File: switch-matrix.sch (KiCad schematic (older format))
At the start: 31 parts, among them P1 SW_0, P2 SW_1, P3 SW_2, P4 SW_3, Q1 NPN, Q2 NPN, Q3 NPN, Q4 NPN, U1 74HC14

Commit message: changed the controller adding some shift registers
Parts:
- renumbered C2 to C1, C3 to C2, C4 to C3, C5 to C4, C1 to C5, D5 to D1, D2 to D10, D3 to D11, D4 to D12, D7 to D2, D9 to D3, D11 to D4, D6 to D5, D8 to D6, D10 to D7, D12 to D8, D1 to D9, P3 to P2, P2 to P3, RP3 to RP2, RP5 to RP3, RP2 to RP5
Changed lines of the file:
@@
-EESchema Schematic File Version 2  date 4/16/2013 9:07:53 PM
+EESchema Schematic File Version 2  date 4/17/2013 1:22:00 AM
 LIBS:power
 LIBS:device
@@
 LIBS:pinball-power
 LIBS:dips-s
+LIBS:Gajda_cmosieee
+LIBS:Gajda_ttlieee
 LIBS:base-module-cache
 EELAYER 27 0
@@
 $EndComp
 $Comp
-L R_PACK4 RP3
+L R_PACK4 RP2
 U 1 1 51644B00
 P 2000 2300
-F 0 "RP3" H 2000 2750 40  0000 C CNN
+F 0 "RP2" H 2000 2750 40  0000 C CNN
 F 1 "R_PACK4" H 2000 2250 40  0000 C CNN
 F 2 "~" H 2000 2300 60  0000 C CNN
@@
 $EndComp
 $Comp
-L R_PACK4 RP5
+L R_PACK4 RP3
 U 1 1 51644B0F
 P 2000 3550
-F 0 "RP5" H 2000 4000 40  0000 C CNN
+F 0 "RP3" H 2000 4000 40  0000 C CNN
 F 1 "R_PACK4" H 2000 3500 40  0000 C CNN
 F 2 "~" H 2000 3550 60  0000 C CNN
@@
 $EndComp
 $Comp
-L R_PACK4 RP2
+L R_PACK4 RP5
 U 1 1 51644B2D
 P 6550 1900
-F 0 "RP2" H 6550 2350 40  0000 C CNN
+F 0 "RP5" H 6550 2350 40  0000 C CNN
 F 1 "R_PACK4" H 6550 1850 40  0000 C CNN
 F 2 "~" H 6550 1900 60  0000 C CNN
@@
 $EndComp
 $Comp
-L ZENERSMALL D1
+L ZENERSMALL D9
 U 1 1 51644B4B
 P 6650 3050
-F 0 "D1" H 6650 3150 40  0000 C CNN
+F 0 "D9" H 6650 3150 40  0000 C CNN
 F 1 "ZENERSMALL" H 6650 2950 30  0000 C CNN
 F 2 "~" H 6650 3050 60  0000 C CNN
@@
 $EndComp
 $Comp
-L ZENERSMALL D2
+L ZENERSMALL D10
 U 1 1 51644B5A
 P 7150 3050
-F 0 "D2" H 7150 3150 40  0000 C CNN
+F 0 "D10" H 7150 3150 40  0000 C CNN
 F 1 "ZENERSMALL" H 7150 2950 30  0000 C CNN
 F 2 "~" H 7150 3050 60  0000 C CNN
@@
 $EndComp
 $Comp
-L ZENERSMALL D3
+L ZENERSMALL D11
 U 1 1 51644B69
 P 7650 3050
-F 0 "D3" H 7650 3150 40  0000 C CNN
+F 0 "D11" H 7650 3150 40  0000 C CNN
 F 1 "ZENERSMALL" H 7650 2950 30  0000 C CNN
 F 2 "~" H 7650 3050 60  0000 C CNN
@@
 $EndComp
 $Comp
-L ZENERSMALL D4
+L ZENERSMALL D12
 U 1 1 51644B78
 P 8150 3050
-F 0 "D4" H 8150 3150 40  0000 C CNN
+F 0 "D12" H 8150 3150 40  0000 C CNN
 F 1 "ZENERSMALL" H 8150 2950 30  0000 C CNN
 F 2 "~" H 8150 3050 60  0000 C CNN
@@
 $EndComp
 $Comp
-L C C2
+L C C1
 U 1 1 51644B87
 P 6850 3050
-F 0 "C2" H 6850 3150 40  0000 L CNN
+F 0 "C1" H 6850 3150 40  0000 L CNN
 F 1 "CYA" H 6856 2965 40  0000 L CNN
 F 2 "~" H 6888 2900 30  0000 C CNN
@@
 $EndComp
 $Comp
-L C C3
+L C C2
 U 1 1 51644B96
 P 7350 3050
-F 0 "C3" H 7350 3150 40  0000 L CNN
+F 0 "C2" H 7350 3150 40  0000 L CNN
 F 1 "CYA" H 7356 2965 40  0000 L CNN
 F 2 "~" H 7388 2900 30  0000 C CNN
@@
 $EndComp
 $Comp
-L C C4
+L C C3
 U 1 1 51644BA5
 P 7850 3050
-F 0 "C4" H 7850 3150 40  0000 L CNN
+F 0 "C3" H 7850 3150 40  0000 L CNN
 F 1 "CYA" H 7856 2965 40  0000 L CNN
 F 2 "~" H 7888 2900 30  0000 C CNN
@@
 $EndComp
 $Comp
-L C C5
+L C C4
 U 1 1 51644BB4
 P 8350 3050
-F 0 "C5" H 8350 3150 40  0000 L CNN
+F 0 "C4" H 8350 3150 40  0000 L CNN
 F 1 "CYA" H 8356 2965 40  0000 L CNN
 F 2 "~" H 8388 2900 30  0000 C CNN
@@
 $EndComp
 $Comp
-L GND #PWR7
+L GND #PWR4
 U 1 1 51644E3A
 P 4000 3300
-F 0 "#PWR7" H 4000 3300 30  0001 C CNN
+F 0 "#PWR4" H 4000 3300 30  0001 C CNN
 F 1 "GND" H 4000 3230 30  0001 C CNN
 F 2 "" H 4000 3300 60  0000 C CNN
@@
 Connection ~ 6650 3350
 $Comp
-L GND #PWR8
+L GND #PWR5
 U 1 1 51645A06
 P 6650 3450
-F 0 "#PWR8" H 6650 3450 30  0001 C CNN
+F 0 "#PWR5" H 6650 3450 30  0001 C CNN
 F 1 "GND" H 6650 3380 30  0001 C CNN
 F 2 "" H 6650 3450 60  0000 C CNN
@@
 	2250 3100 2250 3500
 $Comp
-L +3.3V #PWR6
+L +3.3V #PWR3
 U 1 1 5164C676
 P 2250 3100
-F 0 "#PWR6" H 2250 3060 30  0001 C CNN
+F 0 "#PWR3" H 2250 3060 30  0001 C CNN
 F 1 "+3.3V" H 2250 3210 30  0000 C CNN
 F 2 "" H 2250 3100 60  0000 C CNN
@@
 $EndComp
 $Comp
-L DOUBLE_SCH_KCOM D5
+L DOUBLE_SCH_KCOM D1
 U 1 1 5164D11F
 P 1300 4200
-F 0 "D5" H 1450 4075 60  0000 C CNN
+F 0 "D1" H 1450 4075 60  0000 C CNN
 F 1 "BAT54C" H 1300 4350 60  0000 C CNN
 F 2 "~" H 1300 4200 60  0000 C CNN
@@
 $EndComp
 $Comp
-L DOUBLE_SCH_KCOM D7
+L DOUBLE_SCH_KCOM D2
 U 1 1 5164D12E
 P 1300 4800
-F 0 "D7" H 1450 4675 60  0000 C CNN
+F 0 "D2" H 1450 4675 60  0000 C CNN
 F 1 "BAT54C" H 1300 4950 60  0000 C CNN
 F 2 "~" H 1300 4800 60  0000 C CNN
@@
 Connection ~ 1300 5100
 $Comp
-L +3.3V #PWR4
+L +3.3V #PWR6
 U 1 1 5164DEBC
 P 9350 1900
-F 0 "#PWR4" H 9350 1860 30  0001 C CNN
+F 0 "#PWR6" H 9350 1860 30  0001 C CNN
 F 1 "+3.3V" H 9350 2010 30  0000 C CNN
 F 2 "" H 9350 1900 60  0000 C CNN
@@
 	9350 1950 9350 1900
 $Comp
-L GND #PWR5
+L GND #PWR7
 U 1 1 5164E19F
 P 9350 2200
-F 0 "#PWR5" H 9350 2200 30  0001 C CNN
+F 0 "#PWR7" H 9350 2200 30  0001 C CNN
 F 1 "GND" H 9350 2130 30  0001 C CNN
 F 2 "" H 9350 2200 60  0000 C CNN
@@
 	9350 2200 9350 2150
 $Comp
-L C C1
+L C C5
 U 1 1 5164E2AD
 P 9850 1550
-F 0 "C1" H 9850 1650 40  0000 L CNN
+F 0 "C5" H 9850 1650 40  0000 L CNN
 F 1 "100n" H 9856 1465 40  0000 L CNN
 F 2 "~" H 9888 1400 30  0000 C CNN
@@
 $EndComp
 $Comp
-L +3.3V #PWR2
+L +3.3V #PWR8
 U 1 1 5164E2B8
 P 9850 1300
-F 0 "#PWR2" H 9850 1260 30  0001 C CNN
+F 0 "#PWR8" H 9850 1260 30  0001 C CNN
 F 1 "+3.3V" H 9850 1410 30  0000 C CNN
 F 2 "" H 9850 1300 60  0000 C CNN
@@
 $EndComp
 $Comp
-L GND #PWR3
+L GND #PWR9
 U 1 1 5164E2BE
 P 9850 1800
-F 0 "#PWR3" H 9850 1800 30  0001 C CNN
+F 0 "#PWR9" H 9850 1800 30  0001 C CNN
 F 1 "GND" H 9850 1730 30  0001 C CNN
 F 2 "" H 9850 1800 60  0000 C CNN
@@
 COL3_POWERED
 $Comp
-L CONN_8 P2
+L CONN_8 P3
 U 1 1 516A14DE
 P 5500 4450
-F 0 "P2" V 5450 4450 60  0000 C CNN
+F 0 "P3" V 5450 4450 60  0000 C CNN
 F 1 "SW_1" V 5550 4450 60  0000 C CNN
 F 2 "" H 5500 4450 60  0000 C CNN
@@
 $EndComp
 $Comp
-L DOUBLE_SCH_KCOM D6
+L DOUBLE_SCH_KCOM D5
 U 1 1 516A14E4
 P 3900 4200
-F 0 "D6" H 4050 4075 60  0000 C CNN
+F 0 "D5" H 4050 4075 60  0000 C CNN
 F 1 "BAT54C" H 3900 4350 60  0000 C CNN
 F 2 "~" H 3900 4200 60  0000 C CNN
@@
 $EndComp
 $Comp
-L DOUBLE_SCH_KCOM D8
+L DOUBLE_SCH_KCOM D6
 U 1 1 516A14EA
 P 3900 4800
-F 0 "D8" H 4050 4675 60  0000 C CNN
+F 0 "D6" H 4050 4675 60  0000 C CNN
 F 1 "BAT54C" H 3900 4950 60  0000 C CNN
 F 2 "~" H 3900 4800 60  0000 C CNN
@@
 COL3_POWERED
 $Comp
-L CONN_8 P3
+L CONN_8 P2
 U 1 1 516A1508
 P 2900 5800
-F 0 "P3" V 2850 5800 60  0000 C CNN
+F 0 "P2" V 2850 5800 60  0000 C CNN
 F 1 "SW_2" V 2950 5800 60  0000 C CNN
 F 2 "" H 2900 5800 60  0000 C CNN
@@
 $EndComp
 $Comp
-L DOUBLE_SCH_KCOM D9
+L DOUBLE_SCH_KCOM D3
 U 1 1 516A150E
 P 1300 5550
-F 0 "D9" H 1450 5425 60  0000 C CNN
+F 0 "D3" H 1450 5425 60  0000 C CNN
 F 1 "BAT54C" H 1300 5700 60  0000 C CNN
 F 2 "~" H 1300 5550 60  0000 C CNN
@@
 $EndComp
 $Comp
-L DOUBLE_SCH_KCOM D11
+L DOUBLE_SCH_KCOM D4
 U 1 1 516A1514
 P 1300 6150
-F 0 "D11" H 1450 6025 60  0000 C CNN
+F 0 "D4" H 1450 6025 60  0000 C CNN
 F 1 "BAT54C" H 1300 6300 60  0000 C CNN
 F 2 "~" H 1300 6150 60  0000 C CNN
@@
 $EndComp
 $Comp
-L DOUBLE_SCH_KCOM D10
+L DOUBLE_SCH_KCOM D7
 U 1 1 516A1538
 P 3900 5550
-F 0 "D10" H 4050 5425 60  0000 C CNN
+F 0 "D7" H 4050 5425 60  0000 C CNN
 F 1 "BAT54C" H 3900 5700 60  0000 C CNN
 F 2 "~" H 3900 5550 60  0000 C CNN
@@
 $EndComp
 $Comp
-L DOUBLE_SCH_KCOM D12
+L DOUBLE_SCH_KCOM D8
 U 1 1 516A153E
 P 3900 6150
-F 0 "D12" H 4050 6025 60  0000 C CNN
+F 0 "D8" H 4050 6025 60  0000 C CNN
 F 1 "BAT54C" H 3900 6300 60  0000 C CNN
 F 2 "~" H 3900 6150 60  0000 C CNN

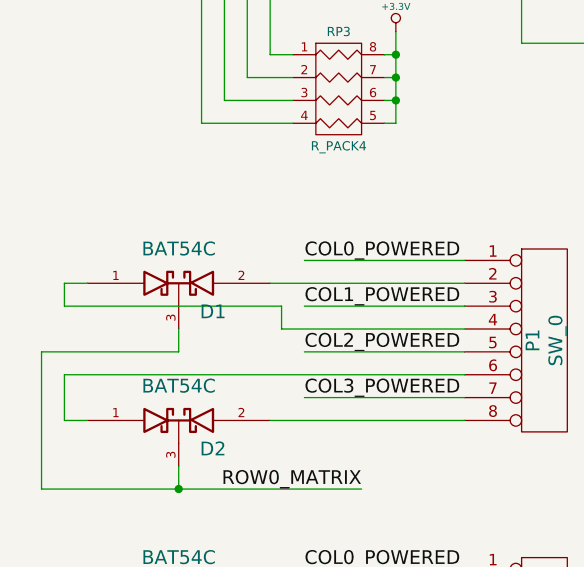
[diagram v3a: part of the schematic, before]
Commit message: added some more info to the different components, changed the pinout for zeeners, and am hating ki-cad for schematic to pads.
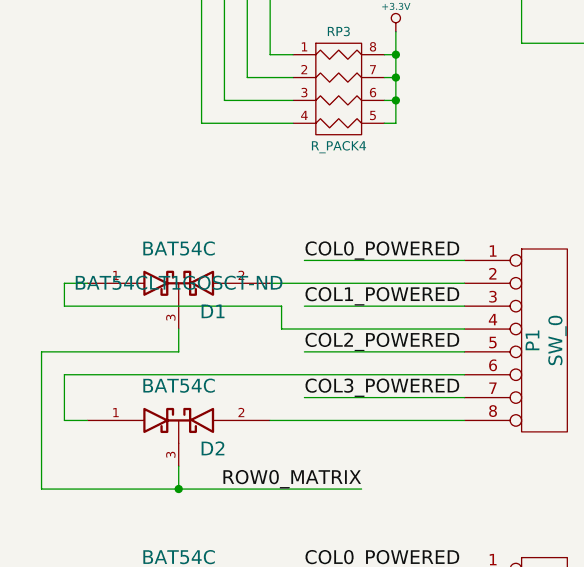
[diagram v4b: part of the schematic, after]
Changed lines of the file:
@@
-EESchema Schematic File Version 2  date 4/18/2013 1:12:38 AM
+EESchema Schematic File Version 2  date 4/19/2013 12:46:09 AM
 LIBS:power
 LIBS:device
@@
 Sheet 2 10
 Title ""
-Date "18 apr 2013"
+Date "19 apr 2013"
 Rev ""
 Comp ""
@@
 F 1 "ZENERSMALL" H 6650 2950 30  0000 C CNN
 F 2 "~" H 6650 3050 60  0000 C CNN
-F 3 "~" H 6650 3050 60  0000 C CNN
+F 3 "954-BZX84-C3V3235-CHP" H 6650 3050 60  0000 C CNN
 	1    6650 3050
 	0    -1   -1   0
@@
 F 1 "BAT54C" H 1300 4350 60  0000 C CNN
 F 2 "~" H 1300 4200 60  0000 C CNN
-F 3 "~" H 1300 4200 60  0000 C CNN
+F 3 "BAT54CLT1GOSCT-ND" H 1300 4200 60  0000 C CNN
 	1    1300 4200
 	1    0    0    -1
